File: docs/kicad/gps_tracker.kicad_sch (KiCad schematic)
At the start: 11 parts, among them J1 GNSS: Foxeer M10Q-250 / Beiti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, J2 SIM800C GPRS board, J3 SSD1306 0.96" OLED I2C 0x3C, J4 MicroSD SPI module, J5 Battery Shield V8, 2x18650, J6 BMA400 CJMCU-400 (not fitted 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, SW1 Button (BOOT-style, active lo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, U1 ESP32-S3-WROOM-1 (DevKitC-1)

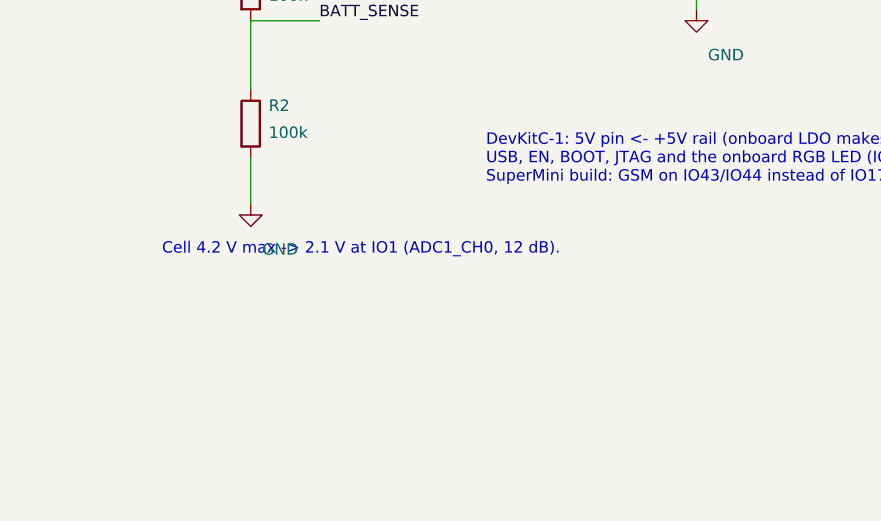
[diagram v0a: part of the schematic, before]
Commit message: Schematic: move the battery-divider note clear of the GND symbol
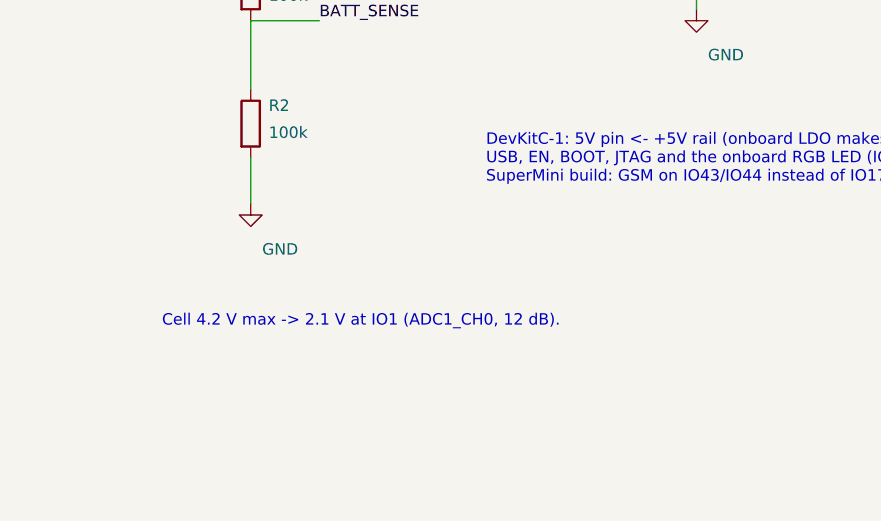
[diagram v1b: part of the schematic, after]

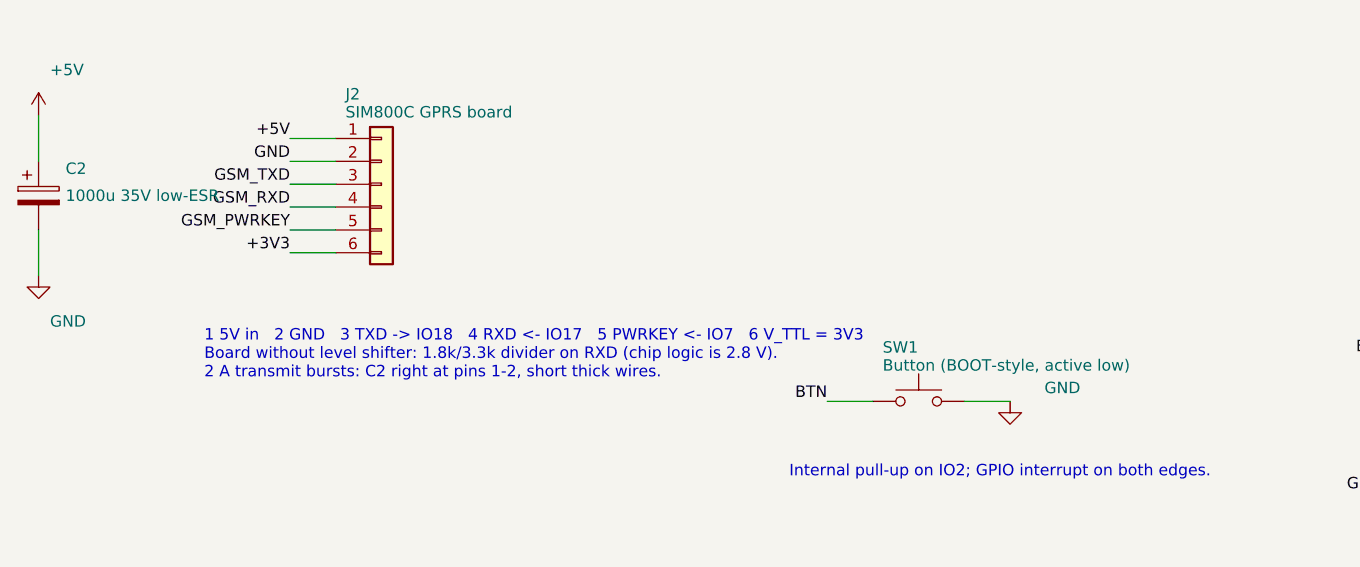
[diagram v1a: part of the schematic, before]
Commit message: Modem supply: 100 uF + ceramic at the board input, the 1000 uF becomes a fallback
The BIGGA SIM800C board carries an 820 uF 6.3 V low-ESR capacitor on the
modem's own 4 V rail, eight times the datasheet minimum, so the transmit
bursts are covered on the board. What remains is the 5 V input to the
board's regulator sagging over wire and contact resistance; 100 uF plus a
100 nF ceramic at the board's input pins and short thick wires handle
that. The 1000 uF stays in the drawer unless the boot line ever shows a
brownout. Hardware doc, schematic (C2 value and note) and exports updated;
ERC still clean.
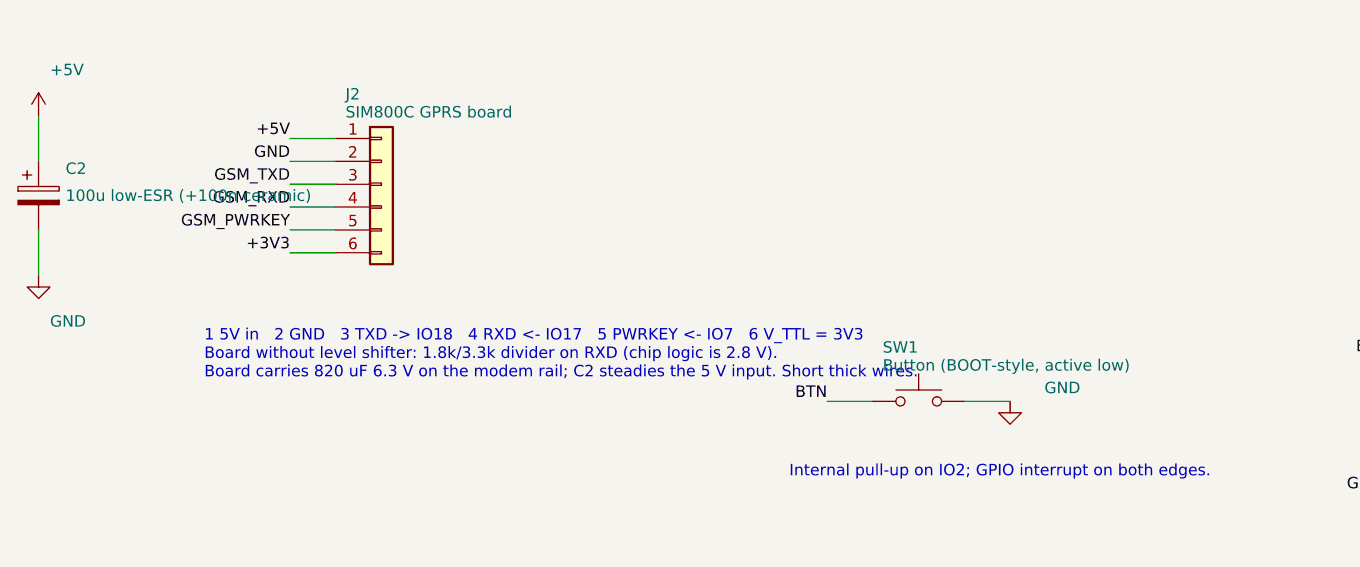
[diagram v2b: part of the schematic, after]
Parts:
- C2: value 1000u 35V low-ESR -> 100u low-ESR (+100n ceramic)
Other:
- note added: "1 5V in 2 GND 3 TXD -> IO18 4 RXD <- IO17 5 PWRKEY <- IO7 6 V_TTL = 3V3 Board without level shifter: 1.8k/3.3k divider on RXD (chip logic is 2.8 V). Board carries 820 uF 6.3 V on the modem rail; C2 steadies the 5 V input. Short thick wires."
- note removed: "1 5V in 2 GND 3 TXD -> IO18 4 RXD <- IO17 5 PWRKEY <- IO7 6 V_TTL = 3V3 Board without level shifter: 1.8k/3.3k divider on RXD (chip logic is 2.8 V). 2 A transmit bursts: C2 right at pins 1-2, short thick wires."

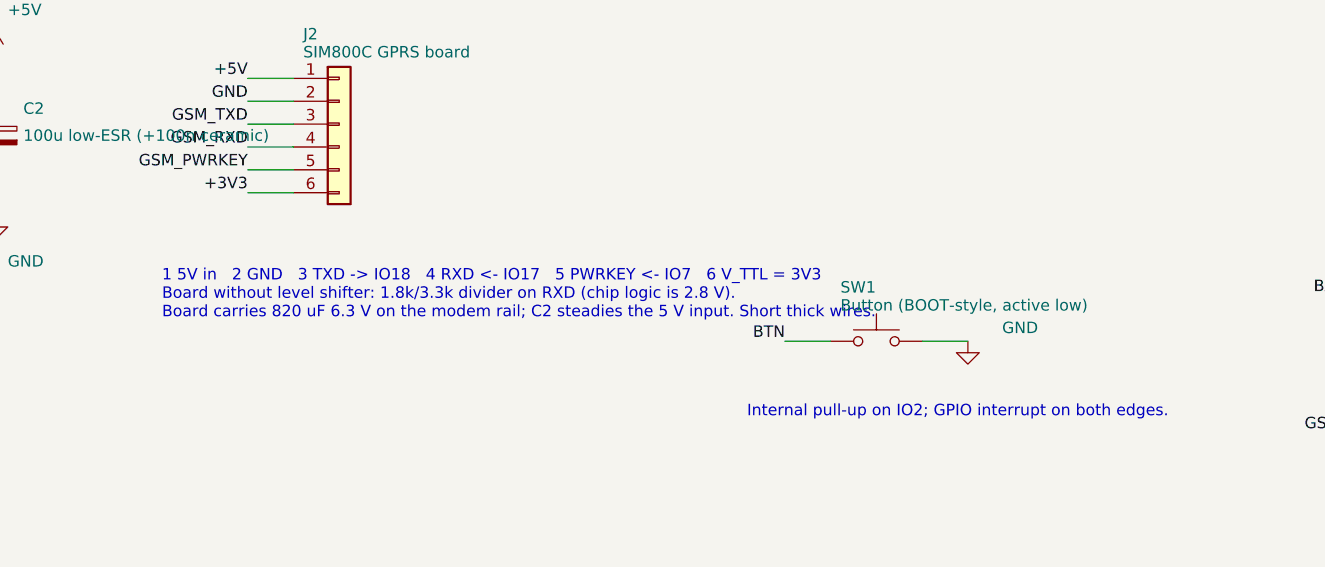
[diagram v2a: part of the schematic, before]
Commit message: SIM800C: probe candidate baud rates at power-on; docs use the board's pin names
The vendor page for this SIM800C board (the common 5V/3.3V TTL board with
Bluetooth and TTS) lists 5V, V_TTL, GND x3, TXD, RXD, PWR, VBAT, DTR, RI,
VRTC and the audio pins. Listings disagree on whether it ships fixed at
9600 baud or in autobaud mode, so powerOn() now tries 115200, 9600, 57600
and 38400 in turn, and only after the modem answers pins it to 115200
with AT+IPR and switches the UART. The hardware doc, the schematic note
and the wiring sheet now name the pin PWR (PWRKEY), state that V_TTL is
the level-shifter reference and that VBAT, DTR, RI, VRTC and audio stay
unconnected.
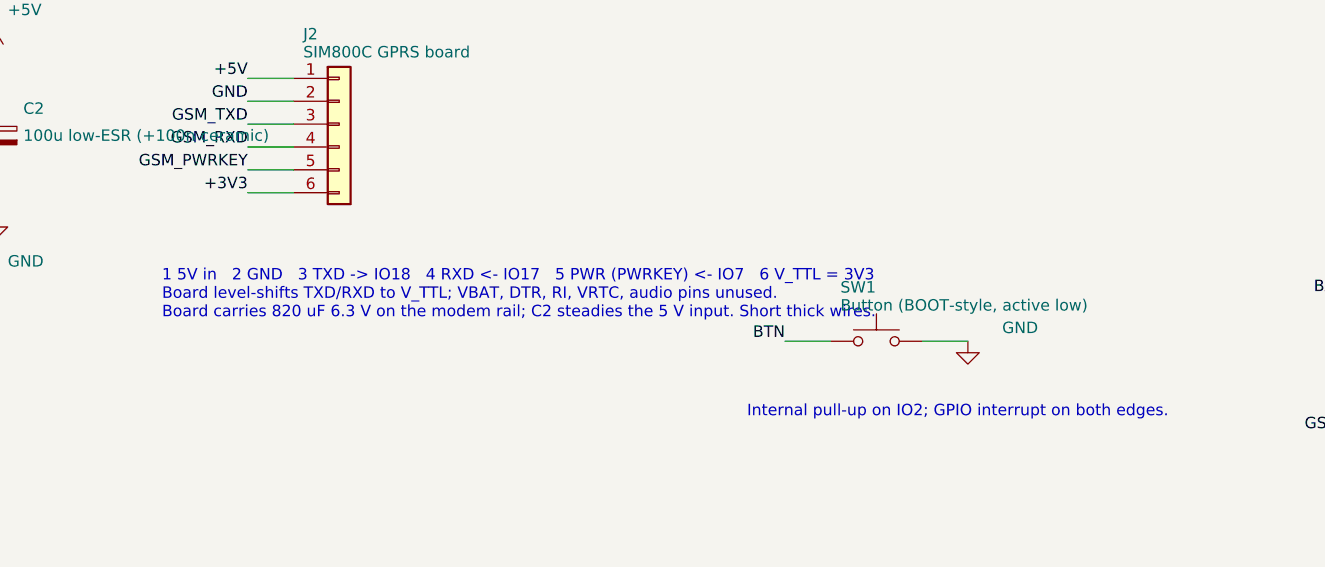
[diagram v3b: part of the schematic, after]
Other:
- note added: "1 5V in 2 GND 3 TXD -> IO18 4 RXD <- IO17 5 PWR (PWRKEY) <- IO7 6 V_TTL = 3V3 Board level-shifts TXD/RXD to V_TTL; VBAT, DTR, RI, VRTC, audio pins unused. Board carries 820 uF 6.3 V on the modem rail; C2 steadies the 5 V input. Short thick wires."
- note removed: "1 5V in 2 GND 3 TXD -> IO18 4 RXD <- IO17 5 PWRKEY <- IO7 6 V_TTL = 3V3 Board without level shifter: 1.8k/3.3k divider on RXD (chip logic is 2.8 V). Board carries 820 uF 6.3 V on the modem rail; C2 steadies the 5 V input. Short thick wires."

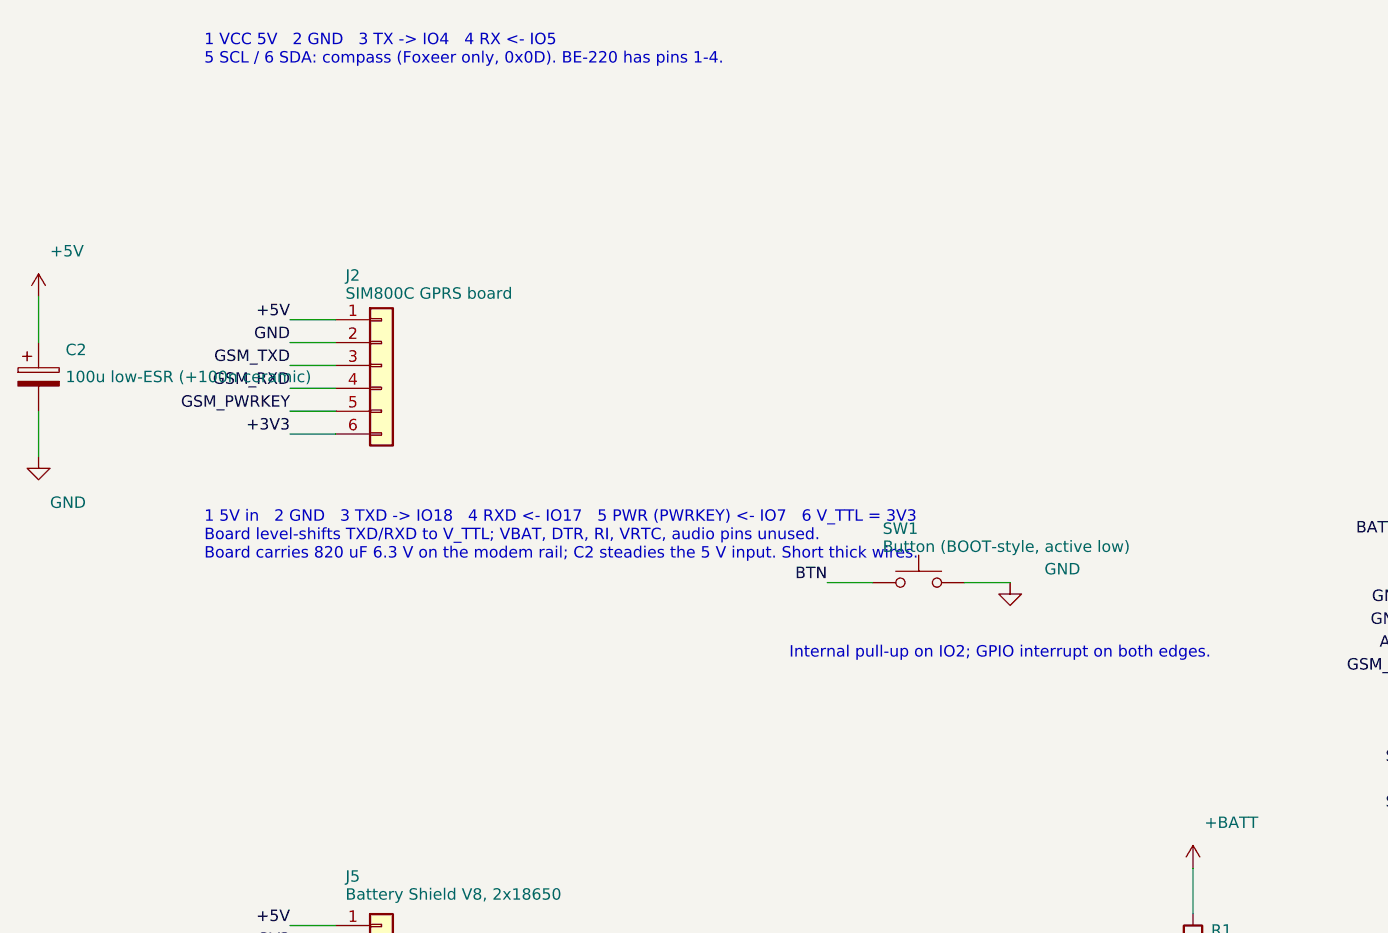
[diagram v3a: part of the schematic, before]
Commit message: BIGGA GSM board: 5 V TX line divided to 3 V, open-drain PWRKEY, real header pinout
The BIGGA GSM schematic (arduino.ua, 2018) shows a MOSFET level shifter
whose high side is pulled up to VCC, so with the required 5 V supply the
board's TX idles at 5 V, above the ESP32-S3's 3.6 V limit. A 6.8 k
resistor from TX to GND forms a divider with the board's 4.7 k pull-up and
brings the high level to about 3.0 V; RX needs nothing because the ESP
drives it against a 47 k pull-up. The board's BOOT pin is the SIM800C
PWRKEY with no auto power-on circuit, so the GPIO driving it is now open
drain and the firmware's existing 'pulse when silent' path is what starts
the modem. VBAT is regulated to 3.64 V by a MIC29302, which leaves little
margin to the 3.4 V reset threshold: the 5 V input must not sag below 4 V,
hence the 100 uF + ceramic at VCC/GND and short thick wires.

Schematic J2 is now the real 12-pin header (GND, TX, RX, BOOT, VCC, NET,
DTR, RING, MICP, MICN, SPKP, SPKN) with R3 on TX; ERC clean. Hardware doc
and the wiring sheet carry the same pinout and the divider.
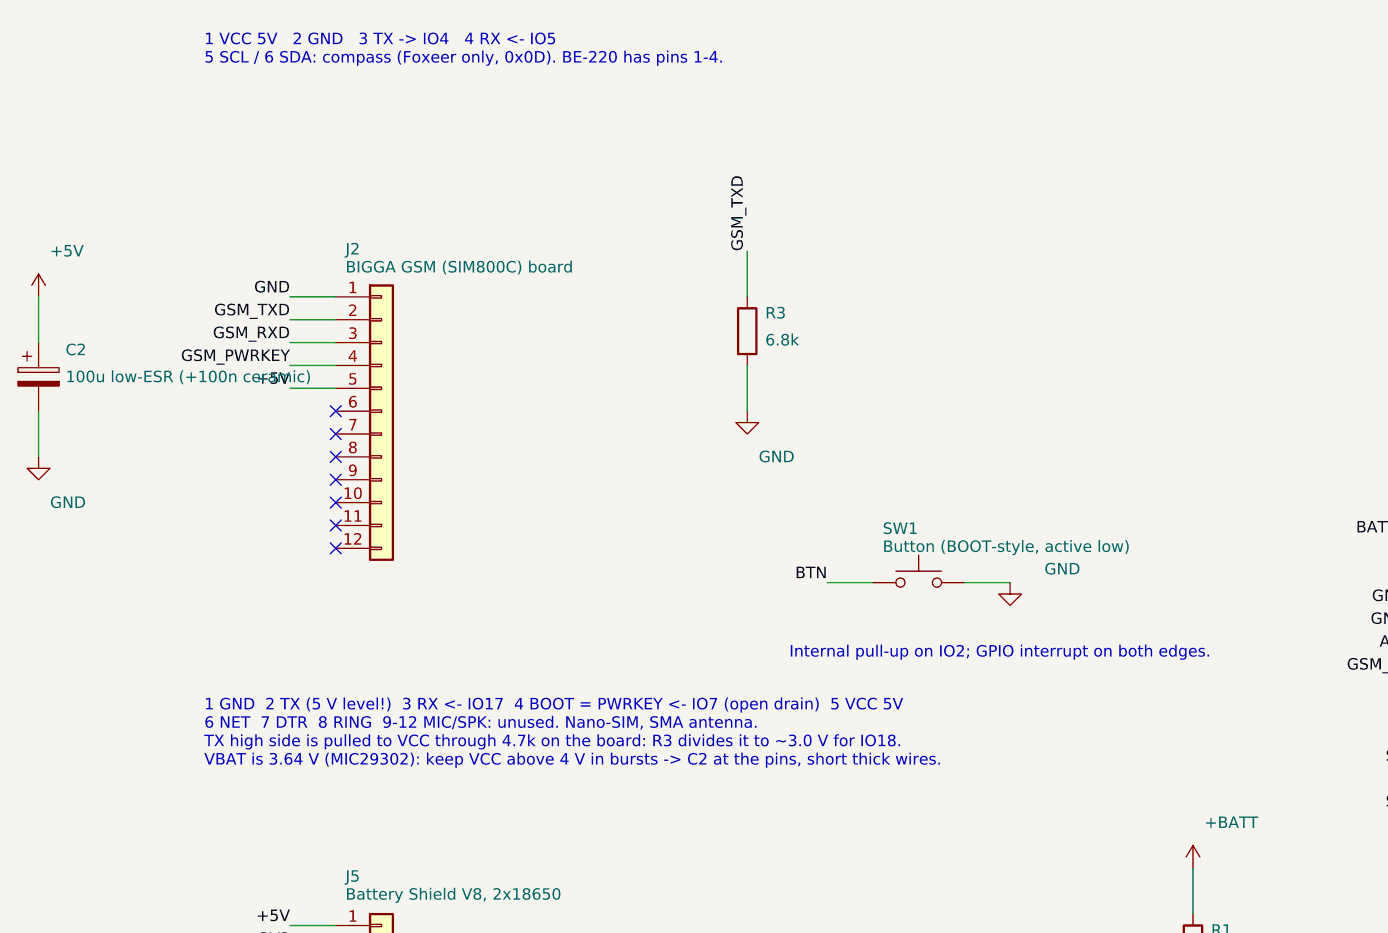
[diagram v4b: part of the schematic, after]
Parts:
- removed J2: SIM800C GPRS board, symbol Connector_Generic:Conn_01x06
- added J2: BIGGA GSM (SIM800C) board, symbol Connector_Generic:Conn_01x12
- added R3: 6.8k, symbol Device:R
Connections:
- net +5V: now also J2.5 (Pin_5)
- net GND: now also J2.1 (Pin_1), R3.2
- net GSM_PWRKEY: now also J2.4 (Pin_4)
- net GSM_RXD: now also J2.3 (Pin_3)
- net GSM_TXD: now also J2.2 (Pin_2), R3.1
- no-connect marks 24 -> 31
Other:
- note added: "1 GND 2 TX (5 V level!) 3 RX <- IO17 4 BOOT = PWRKEY <- IO7 (open drain) 5 VCC 5V 6 NET 7 DTR 8 RING 9-12 MIC/SPK: unused. Nano-SIM, SMA antenna. TX high side is pulled to VCC through 4.7k on the board: R3 divides it to ~3.0 V for IO18. VBAT is 3.64 V (MIC29302): keep VCC above 4 V in bursts -> C2 at the pins, short thick wires."
- note removed: "1 5V in 2 GND 3 TXD -> IO18 4 RXD <- IO17 5 PWR (PWRKEY) <- IO7 6 V_TTL = 3V3 Board level-shifts TXD/RXD to V_TTL; VBAT, DTR, RI, VRTC, audio pins unused. Board carries 820 uF 6.3 V on the modem rail; C2 steadies the 5 V input. Short thick wires."
